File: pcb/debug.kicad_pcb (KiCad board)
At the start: 2 copper layers, 71.7 x 36 mm, 30 parts, among them P1 CONN_01X06, P2 CONN_02X11, P3 CONN_01X08, P4 CONN_02X03, P5 CONN_02X12, P6 CONN_02X03

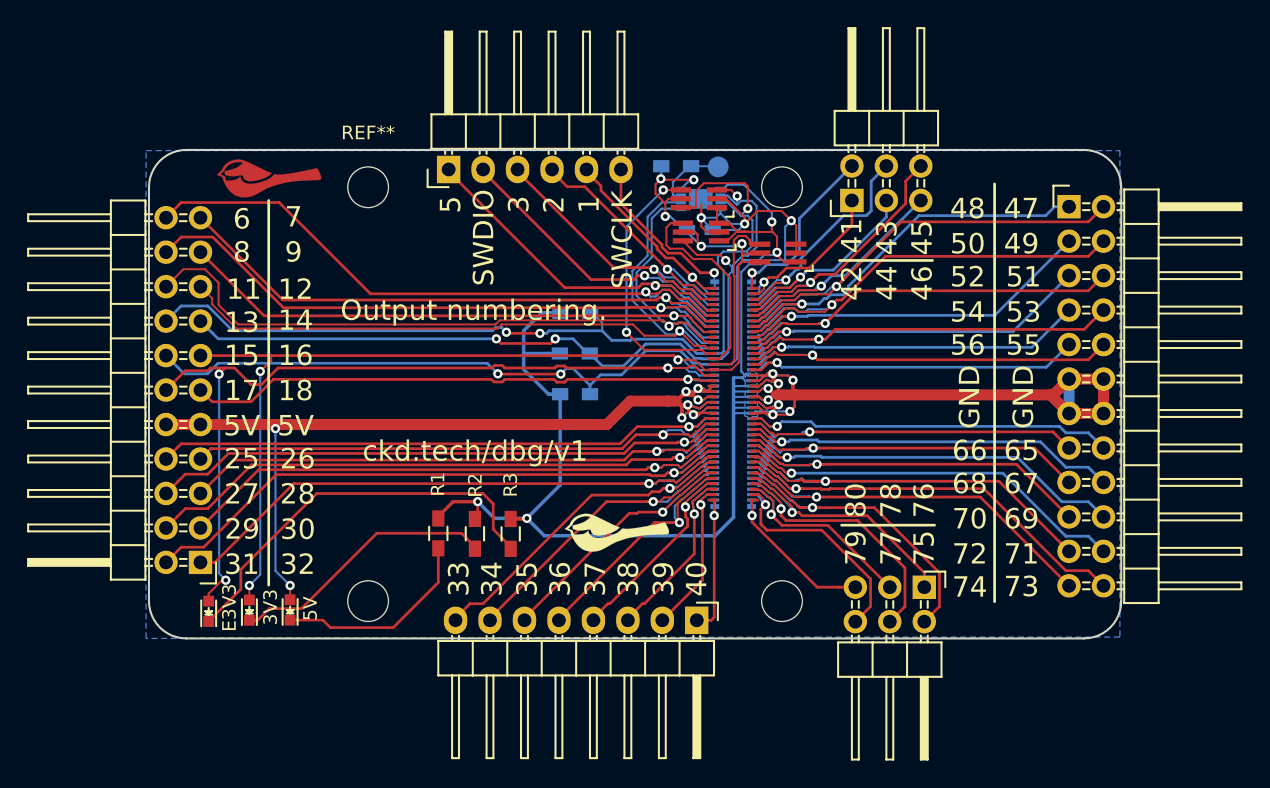
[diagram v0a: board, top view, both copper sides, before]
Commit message: Debug v2 with pin function labels and add inline resistors for SWD lines.
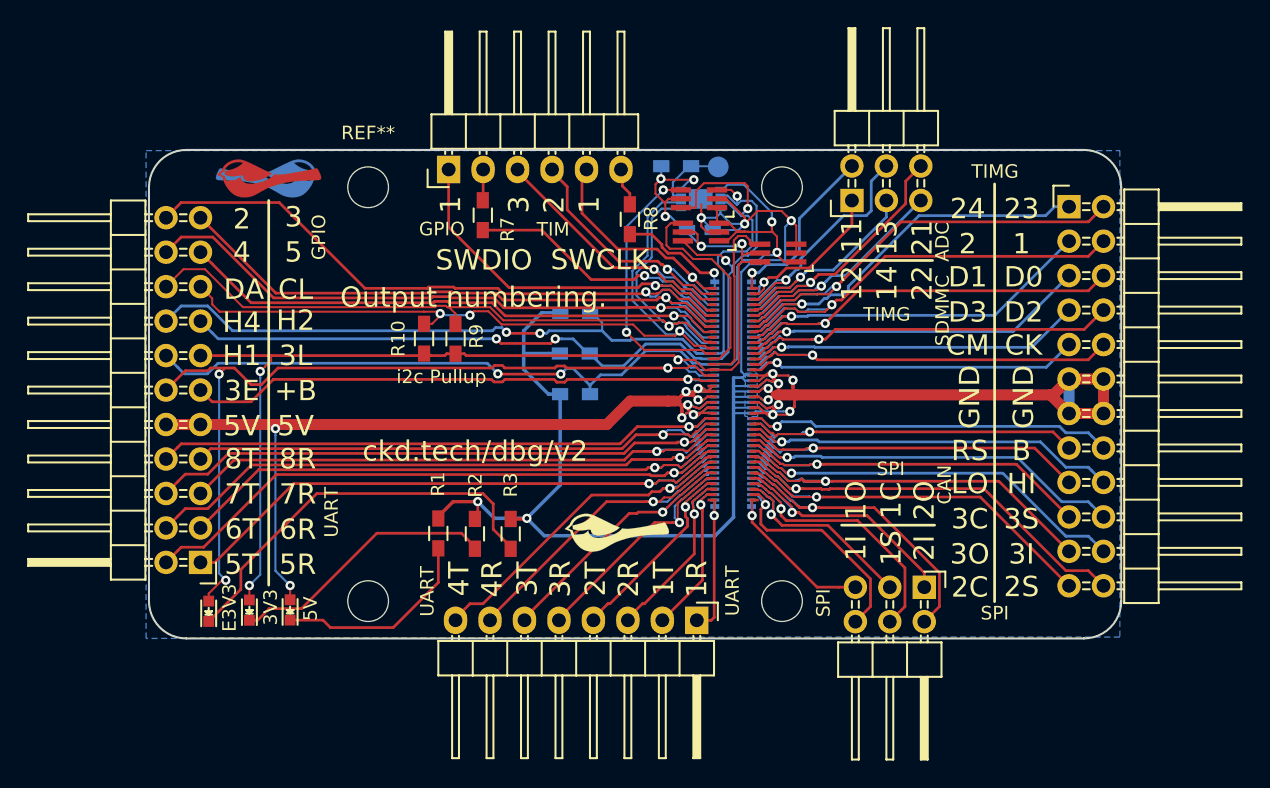
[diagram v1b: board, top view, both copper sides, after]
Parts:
- added G***: Chickadee 3mm, chickadee:chickadee_3mm_fcu, B.Cu at (125.4, 92.1)
- added R10: 10k, Resistors_SMD:R_0603_HandSoldering, F.Cu at (136.9, 103.9)
- added R7: 470, Resistors_SMD:R_0603_HandSoldering, F.Cu at (141.2, 94.8)
- added R8: 470, Resistors_SMD:R_0603_HandSoldering, F.Cu at (152.0, 95.1)
- added R9: 10k, Resistors_SMD:R_0603_HandSoldering, F.Cu at (139.2, 103.9)
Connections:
- P1 pad 2: /ExpansionPort/GPIO1 -> Net-(P1-Pad2)
- P1 pad 6: /ExpansionPort/TIM1 -> Net-(P1-Pad6)
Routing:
- net /ExpansionPort/TIM1: track 12.8 -> 8.66 mm
- net Net-(P1-Pad6): track 0.00 -> 2.84 mm
- net Net-(P1-Pad2): track 0.00 -> 2.43 mm
- net /ExpansionPort/GPIO2: track 29.2 -> 31.6 mm
- net /ExpansionPort/TIM2: track 15.3 -> 17.2 mm
- net /ExpansionPort/GPIO1: track 21.5 -> 19.6 mm
- net /ExpansionPort/i2c_SCL: track 57.5 -> 59.1 mm, vias 1 -> 3
- net /ExpansionPort/TIM3: track 19.9 -> 20.9 mm
- net /ExpansionPort/3V3_0.3A_LL: track 91.5 -> 92.1 mm
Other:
- board text added: "+B"
- board text added: "1C"
- board text added: "1I"
- board text added: "1O"
- board text added: "1R"
- board text added: "1S"
- board text added: "1T"
- board text added: "21"
- board text added: "22"
- board text added: "23"
- board text added: "24"
- board text added: "2C"
- board text added: "2I"
- board text added: "2O"
- board text added: "2R"
- board text added: "2S"
- board text added: "2T"
- board text added: "3C"
- board text added: "3E"
- board text added: "3I"
- board text added: "3L"
- board text added: "3O"
- board text added: "3R"
- board text added: "3S"
- board text added: "3T"
- board text added: "4R"
- board text added: "4T"
- board text added: "5R"
- board text added: "5T"
- board text added: "6R"
- board text added: "6T"
- board text added: "7R"
- board text added: "7T"
- board text added: "8R"
- board text added: "8T"
- board text added: "ADC"
- board text added: "B"
- board text added: "CAN"
- board text added: "CK"
- board text added: "CL"
- board text added: "CM"
- board text added: "D0"
- board text added: "D1"
- board text added: "D2"
- board text added: "D3"
- board text added: "DA"
- board text added: "GPIO"
- board text added: "H1"
- board text added: "H2"
- board text added: "H4"
- board text added: "HI"
- board text added: "LO"
- board text added: "RS"
- board text added: "SDMMC"
- board text added: "SPI"
- board text added: "TIM"
- board text added: "TIMG"
- board text added: "UART"
- board text added: "ckd.tech/dbg/v2"
- board text added: "i2c Pullup"
- board text removed: "10"
- board text removed: "15"
- board text removed: "16"
- board text removed: "17"
- board text removed: "18"
- board text removed: "25"
- board text removed: "26"
- board text removed: "27"
- board text removed: "28"
- board text removed: "29"
- board text removed: "30"
- board text removed: "31"
- board text removed: "32"
- board text removed: "33"
- board text removed: "34"
- board text removed: "35"
- board text removed: "36"
- board text removed: "37"
- board text removed: "38"
- board text removed: "39"
- board text removed: "40"
- board text removed: "41"
- board text removed: "42"
- board text removed: "43"
- board text removed: "44"
- board text removed: "45"
- board text removed: "46"
- board text removed: "47"
- board text removed: "48"
- board text removed: "49"
- board text removed: "50"
- board text removed: "51"
- board text removed: "52"
- board text removed: "53"
- board text removed: "54"
- board text removed: "55"
- board text removed: "56"
- board text removed: "65"
- board text removed: "66"
- board text removed: "67"
- board text removed: "68"
- board text removed: "69"
- board text removed: "7"
- board text removed: "70"
- board text removed: "71"
- board text removed: "72"
- board text removed: "73"
- board text removed: "74"
- board text removed: "75"
- board text removed: "76"
- board text removed: "77"
- board text removed: "78"
- board text removed: "79"
- board text removed: "8"
- board text removed: "80"
- board text removed: "9"
- board text removed: "ckd.tech/dbg/v1"

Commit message: More logos and i2c label.
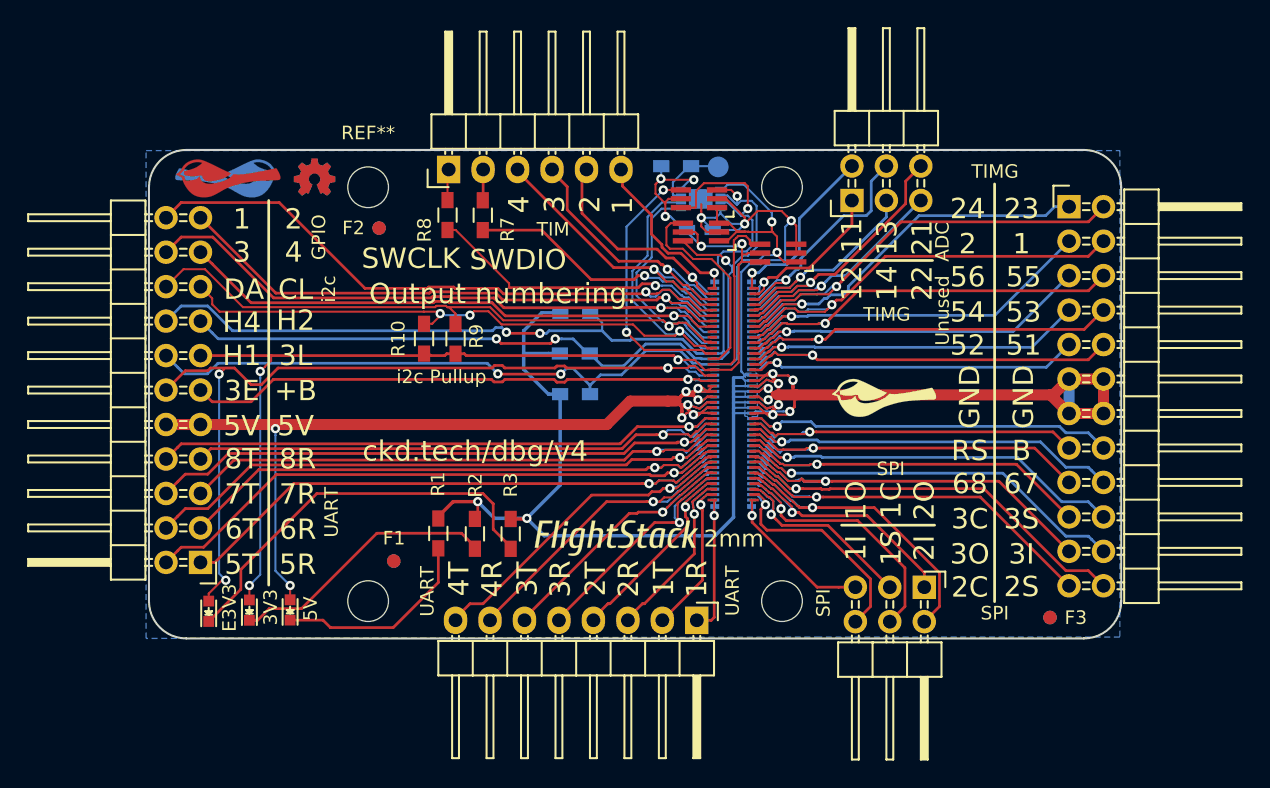
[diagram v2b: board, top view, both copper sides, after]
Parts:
- removed the G*** at (151.2, 118.3)
- added F1: 1mm, macrofab:Fiducial, F.Cu at (134.6, 120.3)
- added F2: 1mm, macrofab:Fiducial, F.Cu at (133.6, 95.8)
- added F3: 1mm, macrofab:Fiducial, F.Cu at (183.0, 124.5)
- added F4: 1mm, macrofab:Fiducial, B.Cu at (134.6, 120.3)
- added F5: 1mm, macrofab:Fiducial, B.Cu at (133.6, 95.8)
- added F6: 1mm, macrofab:Fiducial, B.Cu at (183.0, 124.5)
- added G***: LOGO, chickadee:chickadee_3mm_ss, B.Cu at (170.9, 108.3)
- added G***: LOGO, flightstack:flightstack_thin-12mm, B.Cu at (143.9, 116.1)
- added G***: OSHW, oshw:oshw-3mm, B.Cu at (128.8, 92.0)
- added G***: OSHW, oshw:oshw-3mm, F.Cu at (128.8, 92.0)
- added G***: LOGO, chickadee:chickadee_3mm_ss, F.Cu at (170.9, 108.3)
- added G***: LOGO, flightstack:flightstack_thin-12mm, F.Cu at (151.1, 118.6)
- moved R8 13.4 mm to (138.6, 94.8)
- moved G*** 3.00 mm to (122.4, 92.1) (x2)
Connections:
- P1 pad 1: /ExpansionPort/GPIO2 -> Net-(P1-Pad1)
- P1 pad 6: Net-(P1-Pad6) -> /ExpansionPort/TIM1
- PORT_OUT1 pad 1: /ExpansionPort/TIM2 -> /ExpansionPort/TIM1
- PORT_OUT1 pad 2: /ExpansionPort/TIM3 -> /ExpansionPort/TIM2
- PORT_OUT1 pad 3: /ExpansionPort/TIM4 -> /ExpansionPort/TIM3
- PORT_OUT1 pad 4: Net-(PORT_OUT1-Pad4) -> /ExpansionPort/TIM4
- PORT_OUT1 pad 5: /ExpansionPort/GPIO2 -> /ExpansionPort/GPIO3
- PORT_OUT1 pad 6: /ExpansionPort/GPIO3 -> /ExpansionPort/GPIO4
- PORT_OUT1 pad 7: /ExpansionPort/GPIO4 -> /ExpansionPort/GPIO5
- PORT_OUT1 pad 8: /ExpansionPort/GPIO5 -> /ExpansionPort/GPIO6
- PORT_OUT1 pad 9: /ExpansionPort/GPIO6 -> Net-(PORT_OUT1-Pad9)
- R8 pad 1: Net-(P1-Pad6) -> Net-(P1-Pad1)
- R8 pad 2: /ExpansionPort/TIM1 -> /ExpansionPort/GPIO2
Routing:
- net /ExpansionPort/GPIO2: track 31.6 -> 22.5 mm
- net /ExpansionPort/TIM1: track 8.66 -> 14.0 mm
- net Net-(P1-Pad6): track 2.84 -> 0.00 mm
- net Net-(P1-Pad1): track 0.00 -> 2.29 mm
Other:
- board text added: "2mm"
- board text added: "51"
- board text added: "52"
- board text added: "53"
- board text added: "54"
- board text added: "55"
- board text added: "56"
- board text added: "67"
- board text added: "68"
- board text added: "Unused"
- board text added: "ckd.tech/dbg/v4"
- board text added: "i2c"
- board text removed: "CAN"
- board text removed: "CK"
- board text removed: "CM"
- board text removed: "D0"
- board text removed: "D1"
- board text removed: "D2"
- board text removed: "D3"
- board text removed: "HI"
- board text removed: "LO"
- board text removed: "SDMMC"
- board text removed: "ckd.tech/dbg/v2"

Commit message: Rebrand everything to Polystack and increment versions.
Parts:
- removed the G*** at (143.9, 116.1)
- removed the G*** at (151.1, 118.6)
- added svg2mod: G***, polystack:polystack-medium-0.625, B.Cu at (144.8, 115.9)
- added svg2mod: G***, polystack:polystack-medium-0.625, F.Cu at (150.3, 118.5)
- moved G*** 9.00 mm to (119.8, 92.1)
- moved G*** 3.54 mm to (126.0, 92.0)
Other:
- rule pad_to_mask_clearance: 0.2 -> 0.0762

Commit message: Update polystack logo to bold variant and bump version number.
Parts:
- svg2mod (x2): footprint polystack:polystack-medium-0.625 -> polystack:polystack-bold-0.625
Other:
- board text added: "ckd.tech/dbg/v5"
- board text removed: "ckd.tech/dbg/v4"

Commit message: Add license information to many files. PCB design files are CC-BY and code is MIT license.
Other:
- board text added: "Copyright 2016 Chickadee Tech LLC, <add attributions here> This work is licensed under the Creative Commons Attribution 4.0 International License. To view a copy of this license, visit http://creativecommons.org/licenses/by/4.0/ or send a letter to Creative Commons, PO Box 1866, Mountain View, CA 94042, USA."
- board text added: "Remove all Chickadee Tech LLC trademarks before making your own board. The Chickadee logo and Polystack logo are owned by Chickadee Tech LLC. You may license the Polystack logo for free by emailing support@chickadee.tech and receiving express written permission from Chickadee Tech LLC."
- board text added: "The gear logo is a mark designating open source hardware. Remove it if your design does not comply with the open source hardware definition."
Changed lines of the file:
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@@
     (area 107.021139 74.1 209.880954 178)
     (thickness 1.6)
-    (drawings 211)
+    (drawings 219)
     (tracks 1929)
     (zones 0)
@@
     (39 F.Mask user)
     (40 Dwgs.User user)
-    (41 Cmts.User user hide)
-    (42 Eco1.User user hide)
-    (43 Eco2.User user hide)
+    (41 Cmts.User user)
+    (42 Eco1.User user)
+    (43 Eco2.User user)
     (44 Edge.Cuts user)
     (45 Margin user)
@@
       (xy 4.672239 -0.694521)) (layer B.SilkS) (width 0))
   )
+  (gr_text "Copyright 2016 Chickadee Tech LLC, <add attributions here>\n\nThis work is licensed under the Creative Commons Attribution 4.0 International License.\nTo view a copy of this license, visit http://creativecommons.org/licenses/by/4.0/\nor send a letter to Creative Commons, PO Box 1866, Mountain View, CA 94042, USA." (at 177.92 173.35) (layer Cmts.User)
+    (effects (font (size 1.5 1.5) (thickness 0.3)) (justify left))
+  )
+  (gr_line (start 170.35 110.32) (end 144.4 137.46) (layer Cmts.User) (width 0.2))
+  (gr_line (start 144.4 137.29) (end 148.98 119.99) (layer Cmts.User) (width 0.2))
+  (gr_line (start 124.72 94.38) (end 144.4 137.29) (layer Cmts.User) (width 0.2))
+  (gr_text "Remove all Chickadee Tech LLC trademarks\nbefore making your own board. The\nChickadee logo and Polystack logo\nare owned by Chickadee Tech LLC.\n\nYou may license the Polystack logo for\nfree by emailing support@chickadee.tech\nand receiving express written permission\nfrom Chickadee Tech LLC." (at 136.59 148.15) (layer Cmts.User)
+    (effects (font (size 1.5 1.5) (thickness 0.3)) (justify left))
+  )
+  (gr_line (start 125.36 69.89) (end 128.73 90.1) (layer Cmts.User) (width 0.2))
+  (gr_line (start 119.54 90.1) (end 125.36 69.89) (layer Cmts.User) (width 0.2))
+  (gr_text "The gear logo is a mark designating open\nsource hardware. Remove it if your design\ndoes not comply with the open source\nhardware definition." (at 114.8 64.84) (layer Cmts.User)
+    (effects (font (size 1.5 1.5) (thickness 0.3)) (justify left))
+  )
   (gr_text 2mm (at 159.7 118.65) (layer F.SilkS)
     (effects (font (size 1.25 1.25) (thickness 0.2)))
@@
   (gr_line (start 188.25 92.75) (end 188.25 123.25) (angle 90) (layer Edge.Cuts) (width 0.15))
   (gr_line (start 119.35 90) (end 185.5 90) (angle 90) (layer Edge.Cuts) (width 0.15))
-  (gr_text debug (at 187.25 174.25) (layer Cmts.User)
-    (effects (font (size 5 5) (thickness 0.5)) (justify left))
+  (gr_text debug (at 186.78 189.68) (layer Cmts.User)
+    (effects (font (size 3 3) (thickness 0.5)) (justify left))
   )
   (segment (start 118.719599 106.019599) (end 117.856 105.156) (width 0.2032) (layer B.Cu) (net 1))
